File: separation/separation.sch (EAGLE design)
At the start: 0 parts

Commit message: add rp2040
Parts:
- added JP2, JP4: (no value), microbuilder:HEADER-1X7
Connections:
- new net +3V3: JP4.5
- new net A0: JP2.1
- new net A1: JP2.2
- new net A2: JP2.3
- new net A3: JP2.4
- new net GND: JP4.6
- new net MISO: JP4.3
- new net MOSI: JP4.4
- new net RX: JP4.1
- new net SCK: JP4.2
- new net SCL: JP2.6
- new net SDA: JP2.5
- new net TX: JP2.7
- new net VCC: JP4.7
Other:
- note added: "RP2040"

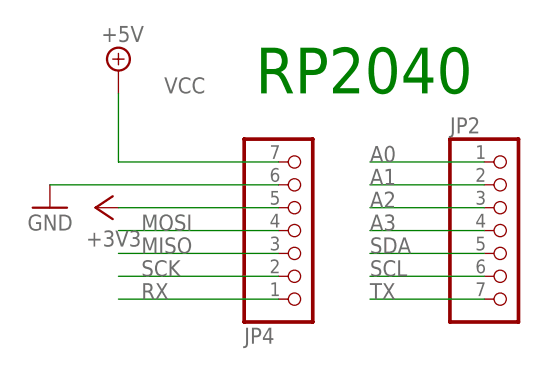
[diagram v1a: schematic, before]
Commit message: remove +5v connector
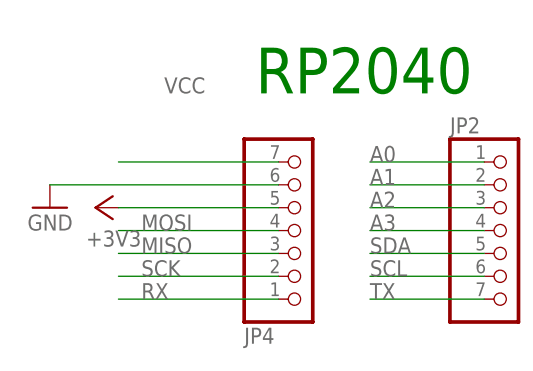
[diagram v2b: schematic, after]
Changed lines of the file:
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@@
 <part name="GND1" library="supply1" library_urn="urn:adsk.eagle:library:371" deviceset="GND" device=""/>
 <part name="JP4" library="microbuilder" deviceset="HEADER-1X7" device=""/>
-<part name="SUPPLY1" library="supply2" library_urn="urn:adsk.eagle:library:372" deviceset="+5V" device=""/>
 <part name="+3V1" library="supply1" library_urn="urn:adsk.eagle:library:371" deviceset="+3V3" device=""/>
 </parts>
@@
 <attribute name="NAME" x="29.21" y="52.705" size="1.778" layer="95" rot="MR180"/>
 <attribute name="VALUE" x="29.21" y="76.2" size="1.778" layer="96" rot="MR180"/>
-</instance>
-<instance part="SUPPLY1" gate="+5V" x="15.24" y="81.28" smashed="yes">
-<attribute name="VALUE" x="13.335" y="84.455" size="1.778" layer="96"/>
 </instance>
 <instance part="+3V1" gate="G$1" x="12.7" y="66.04" smashed="yes" rot="R90">
@@
 <segment>
 <wire x1="33.02" y1="71.12" x2="15.24" y2="71.12" width="0.1524" layer="91"/>
-<wire x1="15.24" y1="71.12" x2="15.24" y2="78.74" width="0.1524" layer="91"/>
 <pinref part="JP4" gate="A" pin="7"/>
-<pinref part="SUPPLY1" gate="+5V" pin="+5V"/>
 <label x="20.32" y="78.74" size="1.778" layer="95"/>
 </segment>

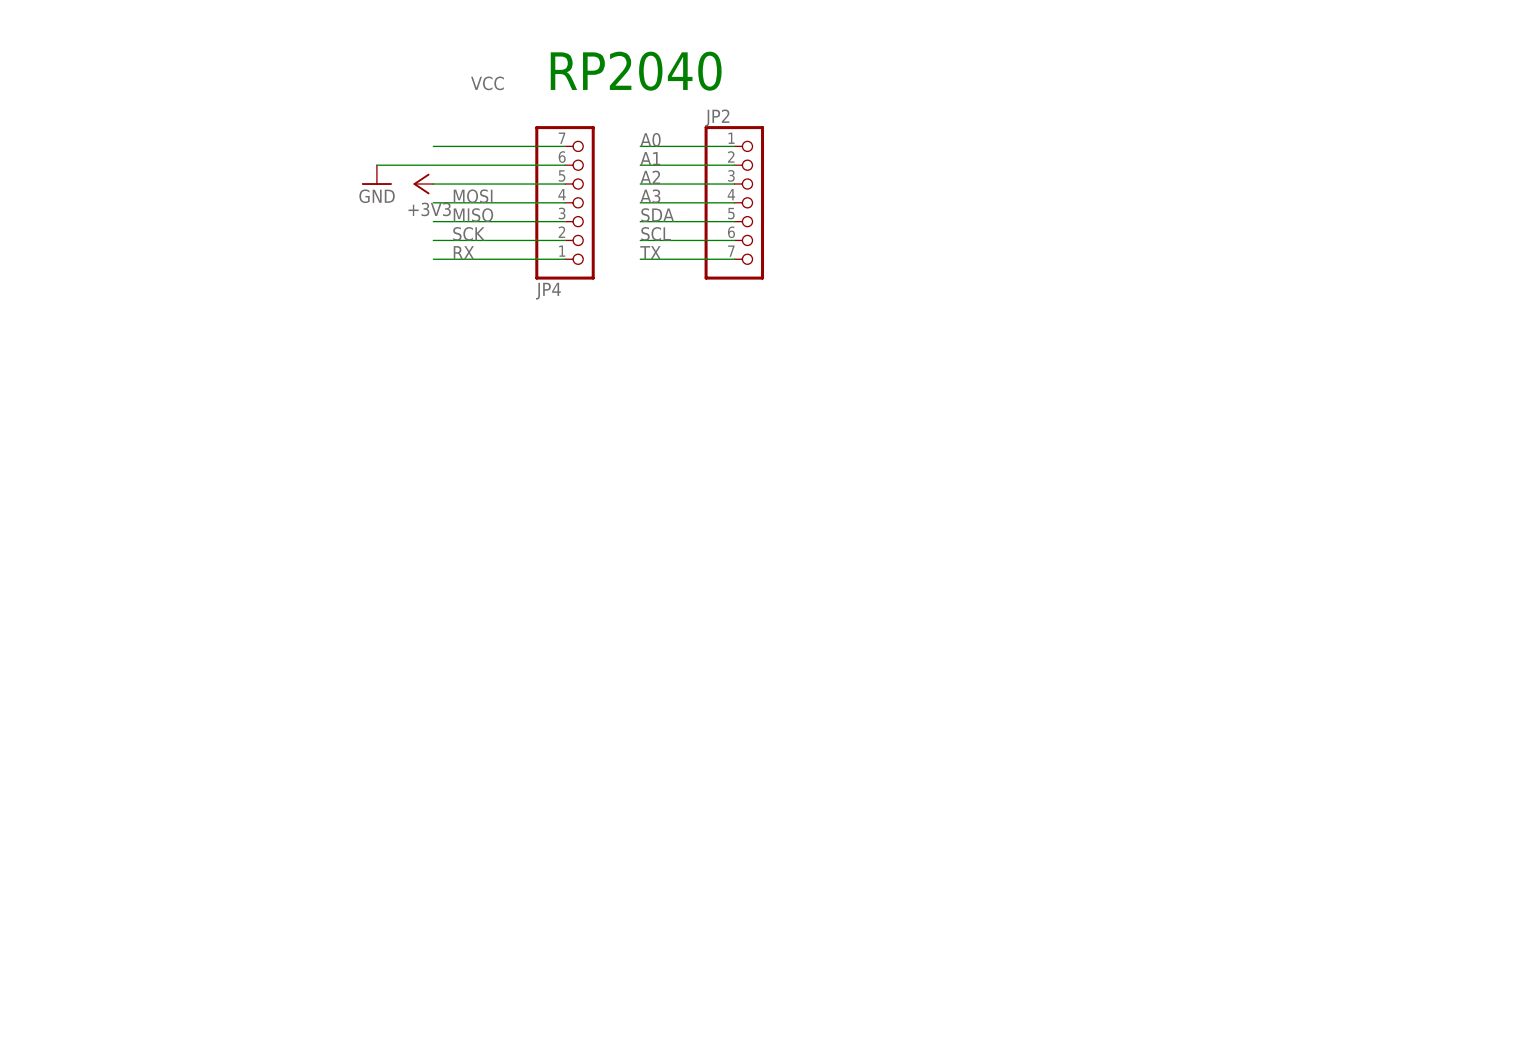
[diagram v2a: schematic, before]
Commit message: add 2x dps
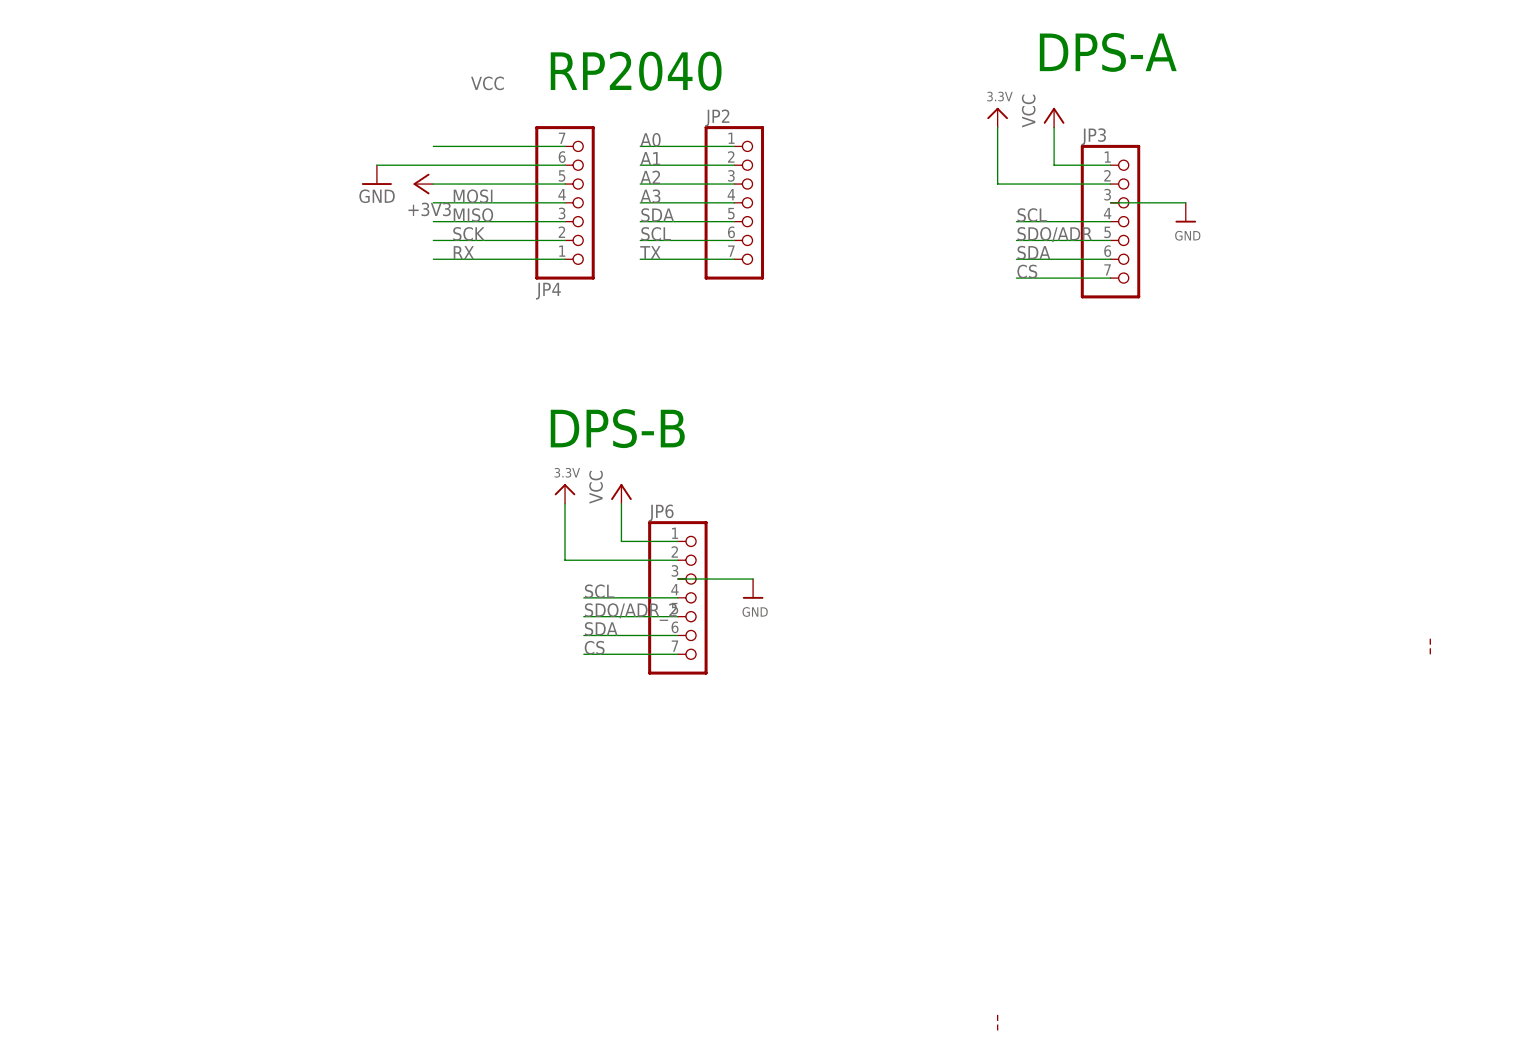
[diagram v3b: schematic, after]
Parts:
- added JP3, JP6: (no value), microbuilder:HEADER-1X770MIL
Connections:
- new net 3.3V: JP3.2, JP6.2
- new net CS: JP3.7, JP6.7
- new net SDO/ADR: JP3.5
- new net SDO/ADR_2: JP6.5
- net GND: now also JP3.3, JP6.3
- net SCL: now also JP3.4, JP6.4
- net SDA: now also JP3.6, JP6.6
- net VCC: now also JP3.1, JP6.1
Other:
- note added: "DPS-A"
- note added: "DPS-B"
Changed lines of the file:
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@@
 <class number="0" name="default" width="0" drill="0">
 </class>
-<class number="1" name="power" width="0.3048" drill="0">
+<class number="1" name="highpower" width="0.3048" drill="0.4826">
+</class>
+<class number="2" name="lowpower" width="0.3048" drill="0.4826">
 </class>
 </classes>
@@
 <part name="JP4" library="microbuilder" deviceset="HEADER-1X7" device=""/>
 <part name="+3V1" library="supply1" library_urn="urn:adsk.eagle:library:371" deviceset="+3V3" device=""/>
+<part name="U$1" library="microbuilder" deviceset="GND" device=""/>
+<part name="U$2" library="microbuilder" deviceset="3.3V" device=""/>
+<part name="P+1" library="supply1" library_urn="urn:adsk.eagle:library:371" deviceset="VCC" device=""/>
+<part name="JP3" library="microbuilder" deviceset="HEADER-1X7" device="70MIL"/>
+<part name="U$5" library="microbuilder" deviceset="GND" device=""/>
+<part name="U$6" library="microbuilder" deviceset="3.3V" device=""/>
+<part name="P+3" library="supply1" library_urn="urn:adsk.eagle:library:371" deviceset="VCC" device=""/>
+<part name="JP6" library="microbuilder" deviceset="HEADER-1X7" device="70MIL"/>
 </parts>
 <sheets>
@@
 <plain>
 <text x="30.48" y="78.74" size="5.08" layer="91">RP2040</text>
+<wire x1="149.86" y1="2.54" x2="149.86" y2="5.08" width="0.1524" layer="94" style="shortdash"/>
+<text x="96.52" y="81.28" size="5.08" layer="91">DPS-A</text>
+<text x="30.48" y="30.48" size="5.08" layer="91">DPS-B</text>
+<wire x1="91.44" y1="-48.26" x2="91.44" y2="-45.72" width="0.1524" layer="94" style="shortdash"/>
 </plain>
 <instances>
@@
 <attribute name="VALUE" x="17.78" y="63.5" size="1.778" layer="96" rot="R180"/>
 </instance>
+<instance part="U$1" gate="G$1" x="116.84" y="60.96" smashed="yes">
+<attribute name="VALUE" x="115.316" y="58.42" size="1.27" layer="96"/>
+</instance>
+<instance part="U$2" gate="G$1" x="91.44" y="76.2" smashed="yes">
+<attribute name="VALUE" x="89.916" y="77.216" size="1.27" layer="96"/>
+</instance>
+<instance part="P+1" gate="VCC" x="99.06" y="76.2" smashed="yes">
+<attribute name="VALUE" x="96.52" y="73.66" size="1.778" layer="96" rot="R90"/>
+</instance>
+<instance part="JP3" gate="A" x="109.22" y="60.96" smashed="yes">
+<attribute name="NAME" x="102.87" y="71.755" size="1.778" layer="95"/>
+<attribute name="VALUE" x="102.87" y="48.26" size="1.778" layer="96"/>
+</instance>
+<instance part="U$5" gate="G$1" x="58.42" y="10.16" smashed="yes">
+<attribute name="VALUE" x="56.896" y="7.62" size="1.27" layer="96"/>
+</instance>
+<instance part="U$6" gate="G$1" x="33.02" y="25.4" smashed="yes">
+<attribute name="VALUE" x="31.496" y="26.416" size="1.27" layer="96"/>
+</instance>
+<instance part="P+3" gate="VCC" x="40.64" y="25.4" smashed="yes">
+<attribute name="VALUE" x="38.1" y="22.86" size="1.778" layer="96" rot="R90"/>
+</instance>
+<instance part="JP6" gate="A" x="50.8" y="10.16" smashed="yes">
+<attribute name="NAME" x="44.45" y="20.955" size="1.778" layer="95"/>
+<attribute name="VALUE" x="44.45" y="-2.54" size="1.778" layer="96"/>
+</instance>
 </instances>
 <busses>
@@
 <pinref part="JP4" gate="A" pin="6"/>
 </segment>
+<segment>
+<pinref part="U$1" gate="G$1" pin="GND"/>
+<wire x1="106.68" y1="63.5" x2="116.84" y2="63.5" width="0.1524" layer="91"/>
+<pinref part="JP3" gate="A" pin="3"/>
+</segment>
+<segment>
+<pinref part="U$5" gate="G$1" pin="GND"/>
+<wire x1="48.26" y1="12.7" x2="58.42" y2="12.7" width="0.1524" layer="91"/>
+<pinref part="JP6" gate="A" pin="3"/>
+</segment>
 </net>
 <net name="MOSI" class="0">
@@
 <label x="43.18" y="58.42" size="1.778" layer="95"/>
 </segment>
+<segment>
+<wire x1="106.68" y1="60.96" x2="93.98" y2="60.96" width="0.1524" layer="91"/>
+<label x="93.98" y="60.96" size="1.778" layer="95"/>
+<pinref part="JP3" gate="A" pin="4"/>
+</segment>
+<segment>
+<wire x1="48.26" y1="10.16" x2="35.56" y2="10.16" width="0.1524" layer="91"/>
+<label x="35.56" y="10.16" size="1.778" layer="95"/>
+<pinref part="JP6" gate="A" pin="4"/>
+</segment>
 </net>
 <net name="SDA" class="0">
@@
 <label x="43.18" y="60.96" size="1.778" layer="95"/>
 </segment>
+<segment>
+<wire x1="106.68" y1="55.88" x2="93.98" y2="55.88" width="0.1524" layer="91"/>
+<label x="93.98" y="55.88" size="1.778" layer="95"/>
+<pinref part="JP3" gate="A" pin="6"/>
+</segment>
+<segment>
+<wire x1="48.26" y1="5.08" x2="35.56" y2="5.08" width="0.1524" layer="91"/>
+<label x="35.56" y="5.08" size="1.778" layer="95"/>
+<pinref part="JP6" gate="A" pin="6"/>
+</segment>
 </net>
 <net name="TX" class="0">
@@
 <label x="20.32" y="78.74" size="1.778" layer="95"/>
 </segment>
-</net>
+<segment>
+<wire x1="106.68" y1="68.58" x2="99.06" y2="68.58" width="0.1524" layer="91"/>
+<wire x1="99.06" y1="68.58" x2="99.06" y2="73.66" width="0.1524" layer="91"/>
+<pinref part="P+1" gate="VCC" pin="VCC"/>
+<pinref part="JP3" gate="A" pin="1"/>
+</segment>
+<segment>
+<wire x1="48.26" y1="17.78" x2="40.64" y2="17.78" width="0.1524" layer="91"/>
+<wire x1="40.64" y1="17.78" x2="40.64" y2="22.86" width="0.1524" layer="91"/>
+<pinref part="P+3" gate="VCC" pin="VCC"/>
+<pinref part="JP6" gate="A" pin="1"/>
+</segment>
+</net>
+<net name="3.3V" class="2">
+<segment>
+<wire x1="106.68" y1="66.04" x2="91.44" y2="66.04" width="0.1524" layer="91"/>
+<wire x1="91.44" y1="66.04" x2="91.44" y2="73.66" width="0.1524" layer="91"/>
+<pinref part="U$2" gate="G$1" pin="3.3V"/>
+<pinref part="JP3" gate="A" pin="2"/>
+</segment>
+<segment>
+<wire x1="48.26" y1="15.24" x2="33.02" y2="15.24" width="0.1524" layer="91"/>
+<wire x1="33.02" y1="15.24" x2="33.02" y2="22.86" width="0.1524" layer="91"/>
+<pinref part="U$6" gate="G$1" pin="3.3V"/>
+<pinref part="JP6" gate="A" pin="2"/>
+</segment>
+</net>
+<net name="SDO/ADR" class="0">
+<segment>
+<wire x1="106.68" y1="58.42" x2="93.98" y2="58.42" width="0.1524" layer="91"/>
+<label x="93.98" y="58.42" size="1.778" layer="95"/>
+<pinref part="JP3" gate="A" pin="5"/>
+</segment>
+</net>
+<net name="CS" class="0">
+<segment>
+<wire x1="106.68" y1="53.34" x2="93.98" y2="53.34" width="0.1524" layer="91"/>
+<label x="93.98" y="53.34" size="1.778" layer="95"/>
+<pinref part="JP3" gate="A" pin="7"/>
+</segment>
+<segment>
+<wire x1="48.26" y1="2.54" x2="35.56" y2="2.54" width="0.1524" layer="91"/>
+<label x="35.56" y="2.54" size="1.778" layer="95"/>
+<pinref part="JP6" gate="A" pin="7"/>
+</segment>
+</net>
+<net name="SDO/ADR_2" class="0">
+<segment>
+<wire x1="48.26" y1="7.62" x2="35.56" y2="7.62" width="0.1524" layer="91"/>
+<label x="35.56" y="7.62" size="1.778" layer="95"/>
+<pinref part="JP6" gate="A" pin="5"/>
+</segment>
+</net>

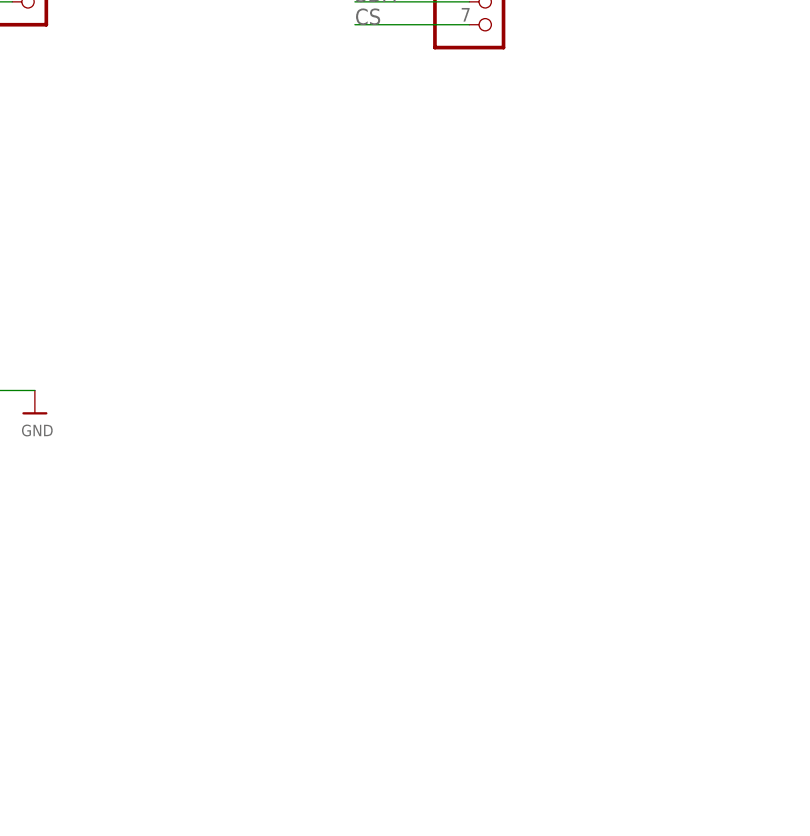
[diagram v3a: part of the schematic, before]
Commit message: add regulator
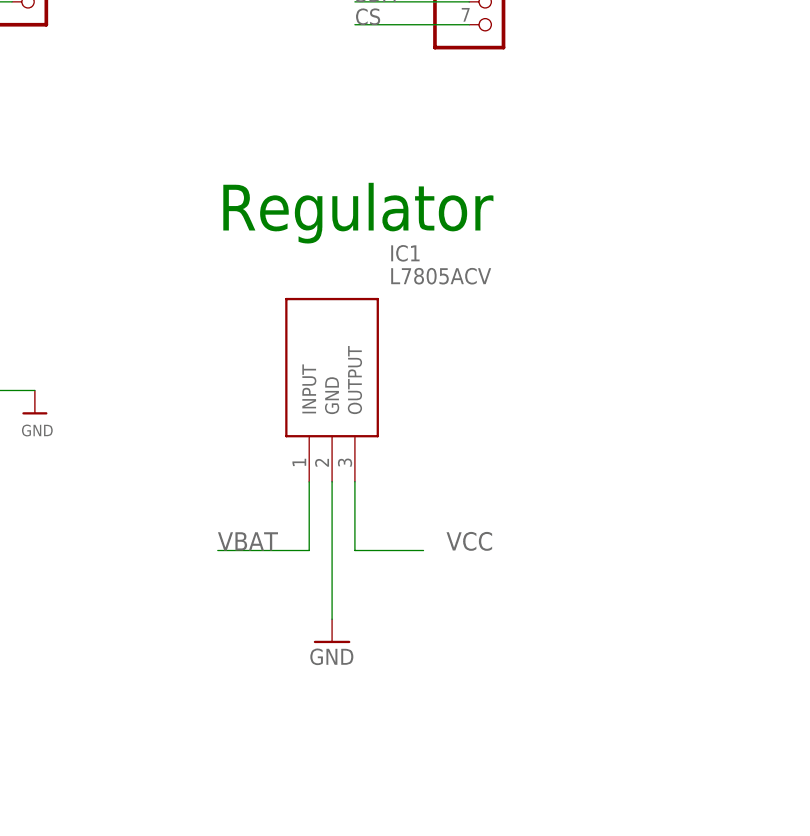
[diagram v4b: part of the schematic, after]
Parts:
- added IC1: L7805ACV, SamacSys_Parts:L7805ACV
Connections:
- new net VBAT: IC1.INPUT
- net GND: now also IC1.GND
- net VCC: now also IC1.OUTPUT
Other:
- note added: "Regulator"
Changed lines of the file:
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@@
 <part name="P+3" library="supply1" library_urn="urn:adsk.eagle:library:371" deviceset="VCC" device=""/>
 <part name="JP6" library="microbuilder" deviceset="HEADER-1X7" device="70MIL"/>
+<part name="IC1" library="SamacSys_Parts" deviceset="L7805ACV" device=""/>
+<part name="GND2" library="supply1" library_urn="urn:adsk.eagle:library:371" deviceset="GND" device=""/>
 </parts>
 <sheets>
@@
 <text x="30.48" y="30.48" size="5.08" layer="91">DPS-B</text>
 <wire x1="91.44" y1="-48.26" x2="91.44" y2="-45.72" width="0.1524" layer="94" style="shortdash"/>
+<text x="78.74" y="30.48" size="5.08" layer="91">Regulator</text>
 </plain>
 <instances>
@@
 <attribute name="VALUE" x="44.45" y="-2.54" size="1.778" layer="96"/>
 </instance>
+<instance part="IC1" gate="G$1" x="88.9" y="2.54" smashed="yes">
+<attribute name="NAME" x="97.79" y="27.94" size="1.778" layer="95" align="center-left"/>
+<attribute name="VALUE" x="97.79" y="25.4" size="1.778" layer="96" align="center-left"/>
+</instance>
+<instance part="GND2" gate="1" x="91.44" y="-15.24" smashed="yes">
+<attribute name="VALUE" x="88.9" y="-17.78" size="1.778" layer="96"/>
+</instance>
 </instances>
 <busses>
@@
 <pinref part="JP6" gate="A" pin="3"/>
 </segment>
+<segment>
+<pinref part="IC1" gate="G$1" pin="GND"/>
+<wire x1="91.44" y1="2.54" x2="91.44" y2="-12.7" width="0.1524" layer="91"/>
+<pinref part="GND2" gate="1" pin="GND"/>
+</segment>
 </net>
 <net name="MOSI" class="0">
@@
 <pinref part="JP6" gate="A" pin="1"/>
 </segment>
+<segment>
+<pinref part="IC1" gate="G$1" pin="OUTPUT"/>
+<wire x1="93.98" y1="2.54" x2="93.98" y2="-5.08" width="0.1524" layer="91"/>
+<wire x1="93.98" y1="-5.08" x2="101.6" y2="-5.08" width="0.1524" layer="91"/>
+<label x="104.14" y="-5.08" size="2.032" layer="95"/>
+</segment>
 </net>
 <net name="3.3V" class="2">
@@
 </segment>
 </net>
+<net name="VBAT" class="0">
+<segment>
+<pinref part="IC1" gate="G$1" pin="INPUT"/>
+<wire x1="88.9" y1="2.54" x2="88.9" y2="-5.08" width="0.1524" layer="91"/>
+<wire x1="88.9" y1="-5.08" x2="78.74" y2="-5.08" width="0.1524" layer="91"/>
+<label x="78.74" y="-5.08" size="2.032" layer="95"/>
+</segment>
+</net>
